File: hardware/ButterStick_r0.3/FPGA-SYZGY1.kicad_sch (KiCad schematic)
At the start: 1 part, among them U4 ECP5UM5G_85_CABGA381

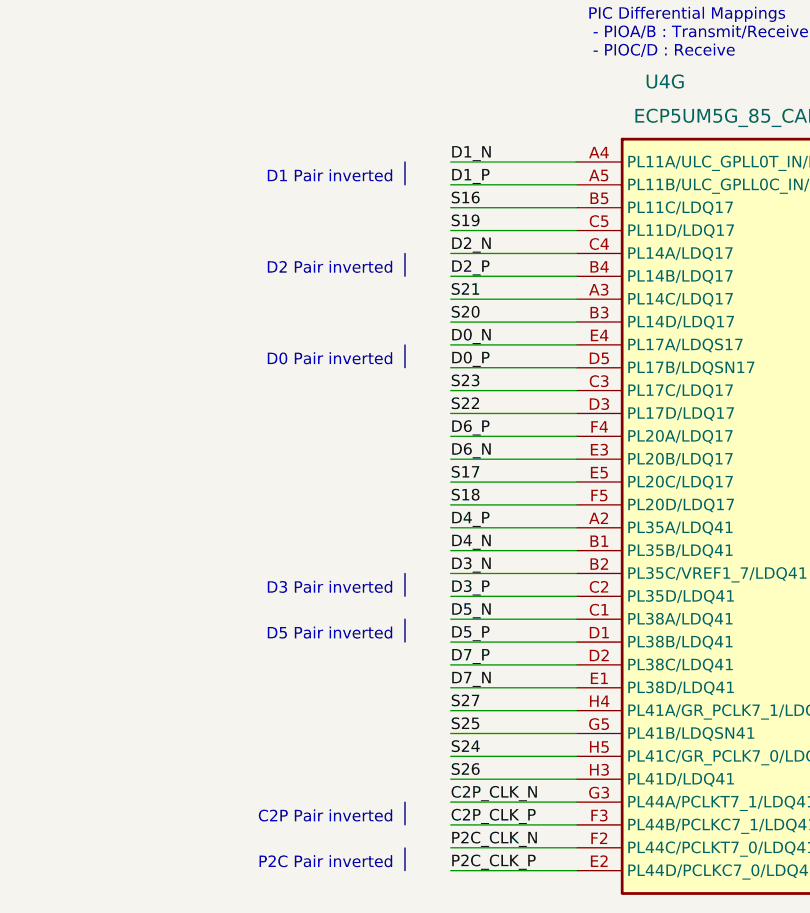
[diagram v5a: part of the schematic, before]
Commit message: hw.r0d3: Length matched all SYZYGY ports
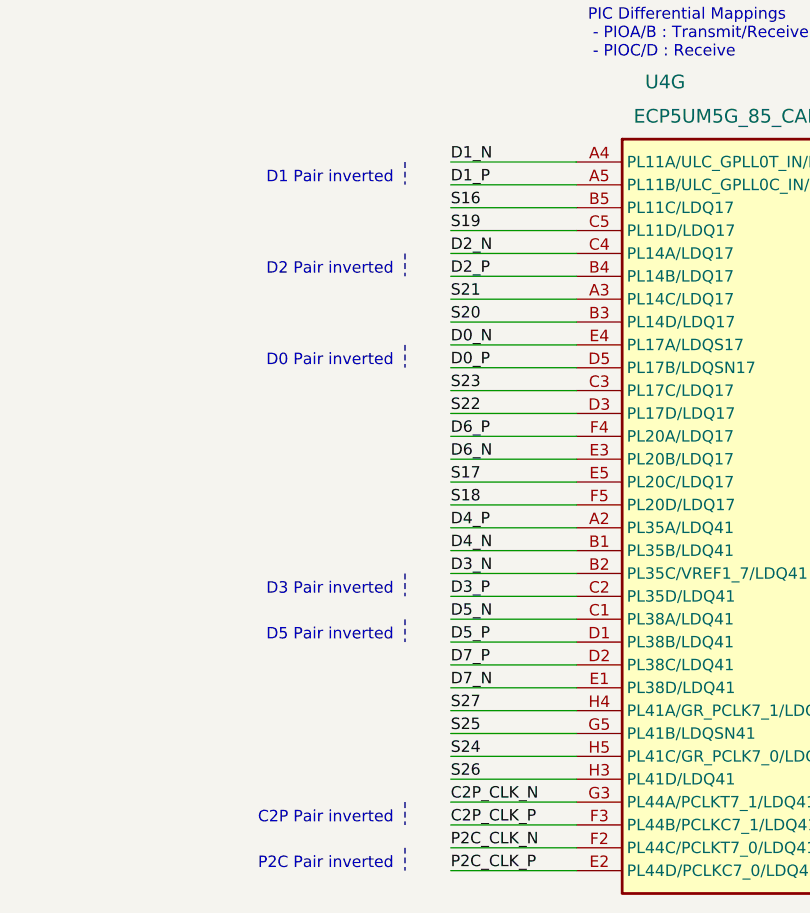
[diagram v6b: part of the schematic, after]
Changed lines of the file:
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@@
-(kicad_sch (version 20200512) (host eeschema "5.99.0-unknown-711fc99~101~ubuntu18.04.1")
-  (page 1 19)
+(kicad_sch (version 20200608) (host eeschema "5.99.0-unknown-08c61e6~101~ubuntu18.04.1")
+  (page 10 19)
   (paper "A4")
   (bus_entry (at 104.14 52.07) (size 2.54 -2.54))
-  (wire (pts (xy 105.41 71.12) (xy 119.38 71.12)))
-  (wire (pts (xy 105.41 73.66) (xy 119.38 73.66)))
-  (wire (pts (xy 105.41 76.2) (xy 119.38 76.2)))
-  (wire (pts (xy 105.41 78.74) (xy 119.38 78.74)))
-  (wire (pts (xy 105.41 81.28) (xy 119.38 81.28)))
-  (wire (pts (xy 105.41 83.82) (xy 119.38 83.82)))
-  (wire (pts (xy 105.41 86.36) (xy 119.38 86.36)))
-  (wire (pts (xy 105.41 88.9) (xy 119.38 88.9)))
-  (wire (pts (xy 105.41 91.44) (xy 119.38 91.44)))
-  (wire (pts (xy 105.41 93.98) (xy 119.38 93.98)))
-  (wire (pts (xy 105.41 96.52) (xy 119.38 96.52)))
-  (wire (pts (xy 105.41 99.06) (xy 119.38 99.06)))
-  (wire (pts (xy 105.41 101.6) (xy 119.38 101.6)))
-  (wire (pts (xy 105.41 104.14) (xy 119.38 104.14)))
-  (wire (pts (xy 105.41 106.68) (xy 119.38 106.68)))
-  (wire (pts (xy 105.41 109.22) (xy 119.38 109.22)))
-  (wire (pts (xy 105.41 111.76) (xy 119.38 111.76)))
-  (wire (pts (xy 105.41 114.3) (xy 119.38 114.3)))
-  (wire (pts (xy 105.41 116.84) (xy 119.38 116.84)))
-  (wire (pts (xy 105.41 119.38) (xy 119.38 119.38)))
-  (wire (pts (xy 105.41 121.92) (xy 119.38 121.92)))
-  (wire (pts (xy 105.41 124.46) (xy 119.38 124.46)))
-  (wire (pts (xy 105.41 127) (xy 119.38 127)))
-  (wire (pts (xy 105.41 129.54) (xy 119.38 129.54)))
-  (wire (pts (xy 105.41 132.08) (xy 119.38 132.08)))
-  (wire (pts (xy 105.41 134.62) (xy 119.38 134.62)))
-  (wire (pts (xy 105.41 137.16) (xy 119.38 137.16)))
-  (wire (pts (xy 105.41 139.7) (xy 119.38 139.7)))
-  (wire (pts (xy 105.41 142.24) (xy 119.38 142.24)))
-  (wire (pts (xy 105.41 144.78) (xy 119.38 144.78)))
-  (wire (pts (xy 105.41 147.32) (xy 119.38 147.32)))
-  (wire (pts (xy 105.41 149.86) (xy 119.38 149.86)))
-  (wire (pts (xy 106.68 49.53) (xy 157.48 49.53)))
-  (wire (pts (xy 157.48 49.53) (xy 157.48 63.5)))
-  (bus (pts (xy 33.02 52.07) (xy 106.68 52.07)))
-  (polyline (pts (xy 100.33 71.12) (xy 100.33 73.66)))
-  (polyline (pts (xy 100.33 81.28) (xy 100.33 83.82)))
-  (polyline (pts (xy 100.33 91.44) (xy 100.33 93.98)))
-  (polyline (pts (xy 100.33 116.84) (xy 100.33 119.38)))
-  (polyline (pts (xy 100.33 121.92) (xy 100.33 124.46)))
-  (polyline (pts (xy 100.33 142.24) (xy 100.33 144.78)))
-  (polyline (pts (xy 100.33 147.32) (xy 100.33 149.86)))
+  (wire (pts (xy 105.41 71.12) (xy 119.38 71.12))
+    (stroke (width 0) (type solid) (color 0 0 0 0))
+  )
+  (wire (pts (xy 105.41 73.66) (xy 119.38 73.66))
+    (stroke (width 0) (type solid) (color 0 0 0 0))
+  )
+  (wire (pts (xy 105.41 76.2) (xy 119.38 76.2))
+    (stroke (width 0) (type solid) (color 0 0 0 0))
+  )
+  (wire (pts (xy 105.41 78.74) (xy 119.38 78.74))
+    (stroke (width 0) (type solid) (color 0 0 0 0))
+  )
+  (wire (pts (xy 105.41 81.28) (xy 119.38 81.28))
+    (stroke (width 0) (type solid) (color 0 0 0 0))
+  )
+  (wire (pts (xy 105.41 83.82) (xy 119.38 83.82))
+    (stroke (width 0) (type solid) (color 0 0 0 0))
+  )
+  (wire (pts (xy 105.41 86.36) (xy 119.38 86.36))
+    (stroke (width 0) (type solid) (color 0 0 0 0))
+  )
+  (wire (pts (xy 105.41 88.9) (xy 119.38 88.9))
+    (stroke (width 0) (type solid) (color 0 0 0 0))
+  )
+  (wire (pts (xy 105.41 91.44) (xy 119.38 91.44))
+    (stroke (width 0) (type solid) (color 0 0 0 0))
+  )
+  (wire (pts (xy 105.41 93.98) (xy 119.38 93.98))
+    (stroke (width 0) (type solid) (color 0 0 0 0))
+  )
+  (wire (pts (xy 105.41 96.52) (xy 119.38 96.52))
+    (stroke (width 0) (type solid) (color 0 0 0 0))
+  )
+  (wire (pts (xy 105.41 99.06) (xy 119.38 99.06))
+    (stroke (width 0) (type solid) (color 0 0 0 0))
+  )
+  (wire (pts (xy 105.41 101.6) (xy 119.38 101.6))
+    (stroke (width 0) (type solid) (color 0 0 0 0))
+  )
+  (wire (pts (xy 105.41 104.14) (xy 119.38 104.14))
+    (stroke (width 0) (type solid) (color 0 0 0 0))
+  )
+  (wire (pts (xy 105.41 106.68) (xy 119.38 106.68))
+    (stroke (width 0) (type solid) (color 0 0 0 0))
+  )
+  (wire (pts (xy 105.41 109.22) (xy 119.38 109.22))
+    (stroke (width 0) (type solid) (color 0 0 0 0))
+  )
+  (wire (pts (xy 105.41 111.76) (xy 119.38 111.76))
+    (stroke (width 0) (type solid) (color 0 0 0 0))
+  )
+  (wire (pts (xy 105.41 114.3) (xy 119.38 114.3))
+    (stroke (width 0) (type solid) (color 0 0 0 0))
+  )
+  (wire (pts (xy 105.41 116.84) (xy 119.38 116.84))
+    (stroke (width 0) (type solid) (color 0 0 0 0))
+  )
+  (wire (pts (xy 105.41 119.38) (xy 119.38 119.38))
+    (stroke (width 0) (type solid) (color 0 0 0 0))
+  )
+  (wire (pts (xy 105.41 121.92) (xy 119.38 121.92))
+    (stroke (width 0) (type solid) (color 0 0 0 0))
+  )
+  (wire (pts (xy 105.41 124.46) (xy 119.38 124.46))
+    (stroke (width 0) (type solid) (color 0 0 0 0))
+  )
+  (wire (pts (xy 105.41 127) (xy 119.38 127))
+    (stroke (width 0) (type solid) (color 0 0 0 0))
+  )
+  (wire (pts (xy 105.41 129.54) (xy 119.38 129.54))
+    (stroke (width 0) (type solid) (color 0 0 0 0))
+  )
+  (wire (pts (xy 105.41 132.08) (xy 119.38 132.08))
+    (stroke (width 0) (type solid) (color 0 0 0 0))
+  )
+  (wire (pts (xy 105.41 134.62) (xy 119.38 134.62))
+    (stroke (width 0) (type solid) (color 0 0 0 0))
+  )
+  (wire (pts (xy 105.41 137.16) (xy 119.38 137.16))
+    (stroke (width 0) (type solid) (color 0 0 0 0))
+  )
+  (wire (pts (xy 105.41 139.7) (xy 119.38 139.7))
+    (stroke (width 0) (type solid) (color 0 0 0 0))
+  )
+  (wire (pts (xy 105.41 142.24) (xy 119.38 142.24))
+    (stroke (width 0) (type solid) (color 0 0 0 0))
+  )
+  (wire (pts (xy 105.41 144.78) (xy 119.38 144.78))
+    (stroke (width 0) (type solid) (color 0 0 0 0))
+  )
+  (wire (pts (xy 105.41 147.32) (xy 119.38 147.32))
+    (stroke (width 0) (type solid) (color 0 0 0 0))
+  )
+  (wire (pts (xy 105.41 149.86) (xy 119.38 149.86))
+    (stroke (width 0) (type solid) (color 0 0 0 0))
+  )
+  (wire (pts (xy 106.68 49.53) (xy 157.48 49.53))
+    (stroke (width 0) (type solid) (color 0 0 0 0))
+  )
+  (wire (pts (xy 157.48 49.53) (xy 157.48 63.5))
+    (stroke (width 0) (type solid) (color 0 0 0 0))
+  )
+  (bus (pts (xy 33.02 52.07) (xy 106.68 52.07))
+    (stroke (width 0) (type solid) (color 0 0 0 0))
+  )
+  (polyline (pts (xy 100.33 71.12) (xy 100.33 73.66))
+    (stroke (width 0) (type dash) (color 0 0 0 0))
+  )
+  (polyline (pts (xy 100.33 81.28) (xy 100.33 83.82))
+    (stroke (width 0) (type dash) (color 0 0 0 0))
+  )
+  (polyline (pts (xy 100.33 91.44) (xy 100.33 93.98))
+    (stroke (width 0) (type dash) (color 0 0 0 0))
+  )
+  (polyline (pts (xy 100.33 116.84) (xy 100.33 119.38))
+    (stroke (width 0) (type dash) (color 0 0 0 0))
+  )
+  (polyline (pts (xy 100.33 121.92) (xy 100.33 124.46))
+    (stroke (width 0) (type dash) (color 0 0 0 0))
+  )
+  (polyline (pts (xy 100.33 142.24) (xy 100.33 144.78))
+    (stroke (width 0) (type dash) (color 0 0 0 0))
+  )
+  (polyline (pts (xy 100.33 147.32) (xy 100.33 149.86))
+    (stroke (width 0) (type dash) (color 0 0 0 0))
+  )
   (text "D1 Pair inverted" (at 99.06 73.66 180)
     (effects (font (size 1.27 1.27)) (justify right bottom))
@@
   )
   (symbol (lib_id "gkl_lattice:ECP5UM5G_85_CABGA381") (at 119.38 71.12 0) (unit 7)
+    (in_bom yes) (on_board yes)
     (property "Reference" "U4" (id 0) (at 127 62.23 0)
       (effects (font (size 1.524 1.524)) (justify left))

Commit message: hw.r0d3: complete first pass of routing
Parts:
- added C27: 100nF, Capacitor_SMD:C_0402_1005Metric, symbol Device:C
- added C28: 10nF, Capacitor_SMD:C_0402_1005Metric, symbol Device:C
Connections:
- net VIO1: now also C27.1, C28.1
- new net GND: C27.2, C28.2
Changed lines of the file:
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@@
-(kicad_sch (version 20200608) (host eeschema "5.99.0-unknown-08c61e6~101~ubuntu18.04.1")
-  (page 1 19)
+(kicad_sch (version 20200618) (host eeschema "5.99.0-unknown-476558e~101~ubuntu18.04.1")
+  (page 10 19)
   (paper "A4")
-  (bus_entry (at 104.14 52.07) (size 2.54 -2.54))
+  (junction (at 157.48 58.42) (diameter 0) (color 0 0 0 0))
+  (junction (at 166.37 64.77) (diameter 0) (color 0 0 0 0))
+  (bus_entry (at 104.14 52.07) (size 2.54 -2.54)
+    (stroke (width 0.1524) (type solid) (color 0 0 0 0))
+  )
   (wire (pts (xy 105.41 71.12) (xy 119.38 71.12))
     (stroke (width 0) (type solid) (color 0 0 0 0))
@@
     (stroke (width 0) (type solid) (color 0 0 0 0))
   )
-  (wire (pts (xy 157.48 49.53) (xy 157.48 63.5))
+  (wire (pts (xy 157.48 49.53) (xy 157.48 58.42))
+    (stroke (width 0) (type solid) (color 0 0 0 0))
+  )
+  (wire (pts (xy 157.48 58.42) (xy 157.48 63.5))
+    (stroke (width 0) (type solid) (color 0 0 0 0))
+  )
+  (wire (pts (xy 157.48 58.42) (xy 166.37 58.42))
+    (stroke (width 0) (type solid) (color 0 0 0 0))
+  )
+  (wire (pts (xy 166.37 58.42) (xy 166.37 64.77))
+    (stroke (width 0) (type solid) (color 0 0 0 0))
+  )
+  (wire (pts (xy 166.37 64.77) (xy 166.37 66.04))
+    (stroke (width 0) (type solid) (color 0 0 0 0))
+  )
+  (wire (pts (xy 166.37 64.77) (xy 176.53 64.77))
+    (stroke (width 0) (type solid) (color 0 0 0 0))
+  )
+  (wire (pts (xy 166.37 73.66) (xy 166.37 74.93))
+    (stroke (width 0) (type solid) (color 0 0 0 0))
+  )
+  (wire (pts (xy 176.53 66.04) (xy 176.53 64.77))
+    (stroke (width 0) (type solid) (color 0 0 0 0))
+  )
+  (wire (pts (xy 176.53 74.93) (xy 176.53 73.66))
     (stroke (width 0) (type solid) (color 0 0 0 0))
   )
@@
     (effects (font (size 1.27 1.27)) (justify right))
   )
+  (symbol (lib_id "gkl_power:GND") (at 166.37 74.93 0) (unit 1)
+    (in_bom yes) (on_board yes)
+    (property "Reference" "#PWR0213" (id 0) (at 166.37 81.28 0)
+      (effects (font (size 1.27 1.27)) hide)
+    )
+    (property "Value" "GND" (id 1) (at 166.4462 78.1304 0))
+    (property "Footprint" "" (id 2) (at 163.83 83.82 0)
+      (effects (font (size 1.27 1.27)) hide)
+    )
+    (property "Datasheet" "" (id 3) (at 166.37 74.93 0)
+      (effects (font (size 1.27 1.27)) hide)
+    )
+  )
+  (symbol (lib_id "gkl_power:GND") (at 176.53 74.93 0) (unit 1)
+    (in_bom yes) (on_board yes)
+    (property "Reference" "#PWR0212" (id 0) (at 176.53 81.28 0)
+      (effects (font (size 1.27 1.27)) hide)
+    )
+    (property "Value" "GND" (id 1) (at 176.6062 78.1304 0))
+    (property "Footprint" "" (id 2) (at 173.99 83.82 0)
+      (effects (font (size 1.27 1.27)) hide)
+    )
+    (property "Datasheet" "" (id 3) (at 176.53 74.93 0)
+      (effects (font (size 1.27 1.27)) hide)
+    )
+  )
+  (symbol (lib_id "Device:C") (at 166.37 69.85 0) (unit 1)
+    (in_bom yes) (on_board yes)
+    (property "Reference" "C27" (id 0) (at 167.64 67.31 0)
+      (effects (font (size 1.27 1.27)) (justify left))
+    )
+    (property "Value" "100nF" (id 1) (at 167.64 72.39 0)
+      (effects (font (size 1.27 1.27)) (justify left))
+    )
+    (property "Footprint" "Capacitor_SMD:C_0402_1005Metric" (id 2) (at 167.3352 73.66 0)
+      (effects (font (size 1.27 1.27)) hide)
+    )
+    (property "Datasheet" "" (id 3) (at 166.37 69.85 0)
+      (effects (font (size 1.27 1.27)) hide)
+    )
+    (property "SN-DK" "1276-1002-1-ND" (id 4) (at 16.51 246.38 0)
+      (effects (font (size 1.27 1.27)) hide)
+    )
+    (property "PN" "CL05B104KP5NNNC" (id 5) (at 16.51 246.38 0)
+      (effects (font (size 1.27 1.27)) hide)
+    )
+    (property "Mfg" "Samsung Electro-Mechanics" (id 6) (at 19.05 245.11 0)
+      (effects (font (size 1.27 1.27)) hide)
+    )
+  )
+  (symbol (lib_id "Device:C") (at 176.53 69.85 0) (unit 1)
+    (in_bom yes) (on_board yes)
+    (property "Reference" "C28" (id 0) (at 177.8 67.31 0)
+      (effects (font (size 1.27 1.27)) (justify left))
+    )
+    (property "Value" "10nF" (id 1) (at 177.8 72.39 0)
+      (effects (font (size 1.27 1.27)) (justify left))
+    )
+    (property "Footprint" "Capacitor_SMD:C_0402_1005Metric" (id 2) (at 177.4952 73.66 0)
+      (effects (font (size 1.27 1.27)) hide)
+    )
+    (property "Datasheet" "" (id 3) (at 176.53 69.85 0)
+      (effects (font (size 1.27 1.27)) hide)
+    )
+    (property "SN-DK" "1276-1002-1-ND" (id 4) (at 26.67 246.38 0)
+      (effects (font (size 1.27 1.27)) hide)
+    )
+    (property "PN" "CL05B103KP5NNNC" (id 5) (at 26.67 246.38 0)
+      (effects (font (size 1.27 1.27)) hide)
+    )
+    (property "Mfg" "Samsung Electro-Mechanics" (id 6) (at 19.05 245.11 0)
+      (effects (font (size 1.27 1.27)) hide)
+    )
+  )
   (symbol (lib_id "gkl_lattice:ECP5UM5G_85_CABGA381") (at 119.38 71.12 0) (unit 7)
